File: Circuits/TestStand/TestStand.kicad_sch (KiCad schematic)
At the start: 43 parts, among them J1 Screw_Terminal_01x07, J2 Screw_Terminal_01x07, J3 Screw_Terminal_01x07, J4 Raspberry_Pi_2_3, Q1 MMBT4403-7-F, Q2 MMBT4403-7-F, Q3 MMBT4403-7-F, U1 HX711, U2 HX711, U3 HX711

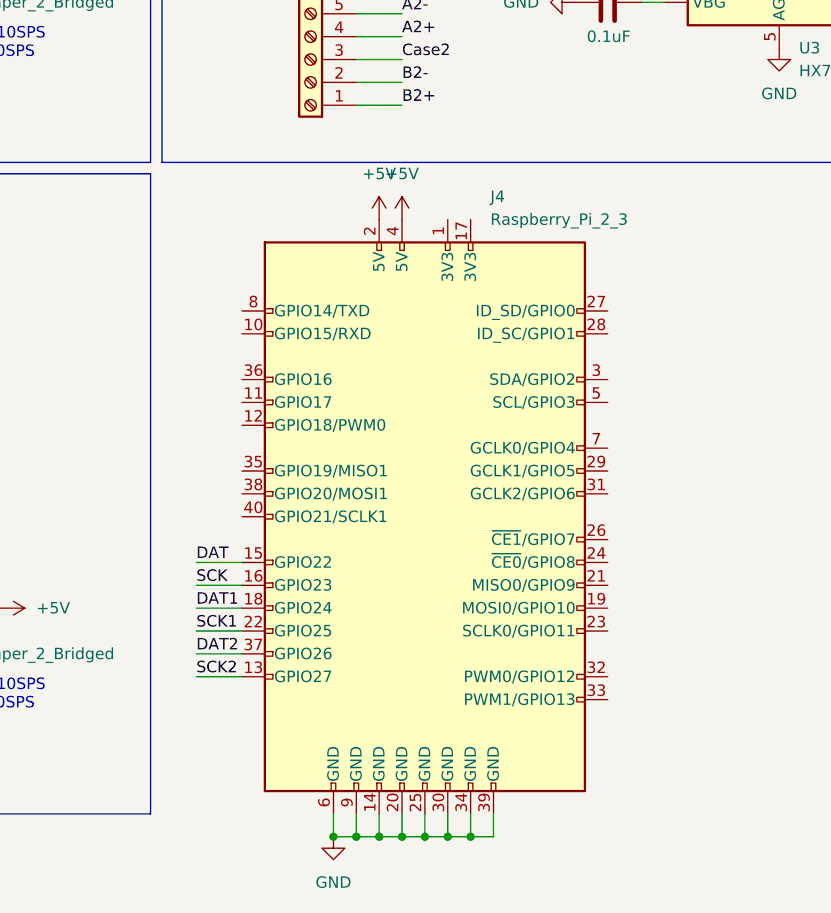
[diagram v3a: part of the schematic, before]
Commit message: Deleted PI, added servos
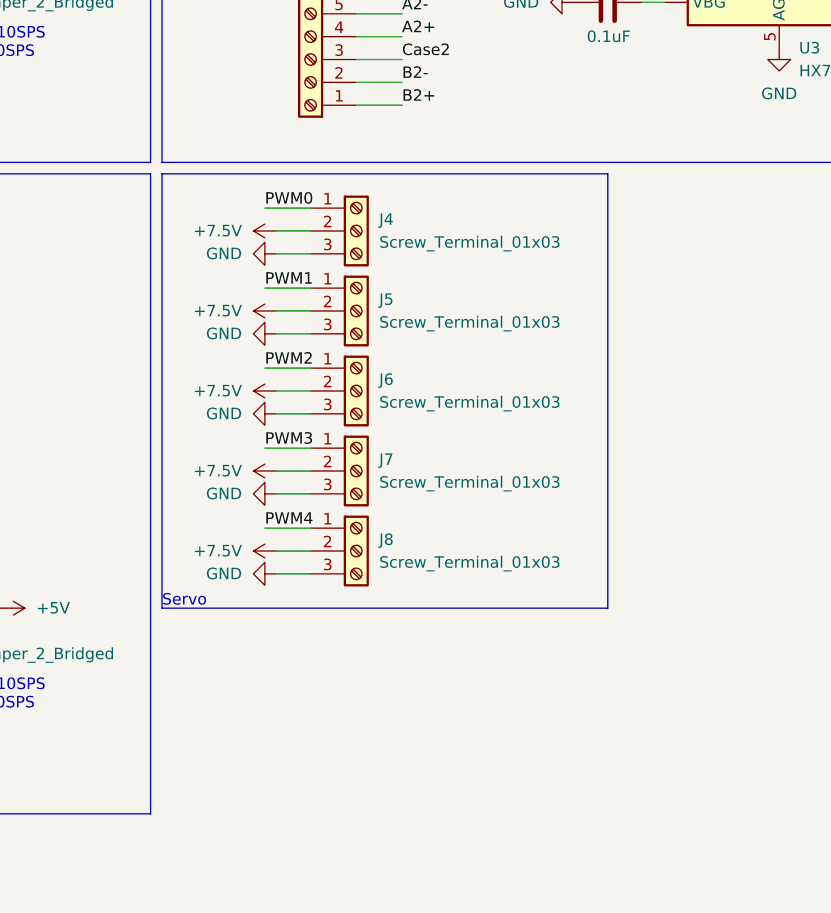
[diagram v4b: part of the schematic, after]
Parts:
- removed J4: Raspberry_Pi_2_3, symbol Connector:Raspberry_Pi_2_3
- added J4, J5, J6, J7, J8: Screw_Terminal_01x03, symbol Connector:Screw_Terminal_01x03
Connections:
- net GND: now also J4.3 (Pin_3), J5.3 (Pin_3), J6.3 (Pin_3), J7.3 (Pin_3), J8.3 (Pin_3)
- new net +7.5V: J4.2 (Pin_2), J5.2 (Pin_2), J6.2 (Pin_2), J7.2 (Pin_2), J8.2 (Pin_2)
- new net PWM0: J4.1 (Pin_1)
- new net PWM1: J5.1 (Pin_1)
- new net PWM2: J6.1 (Pin_1)
- new net PWM3: J7.1 (Pin_1)
- new net PWM4: J8.1 (Pin_1)
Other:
- note added: "Servo"

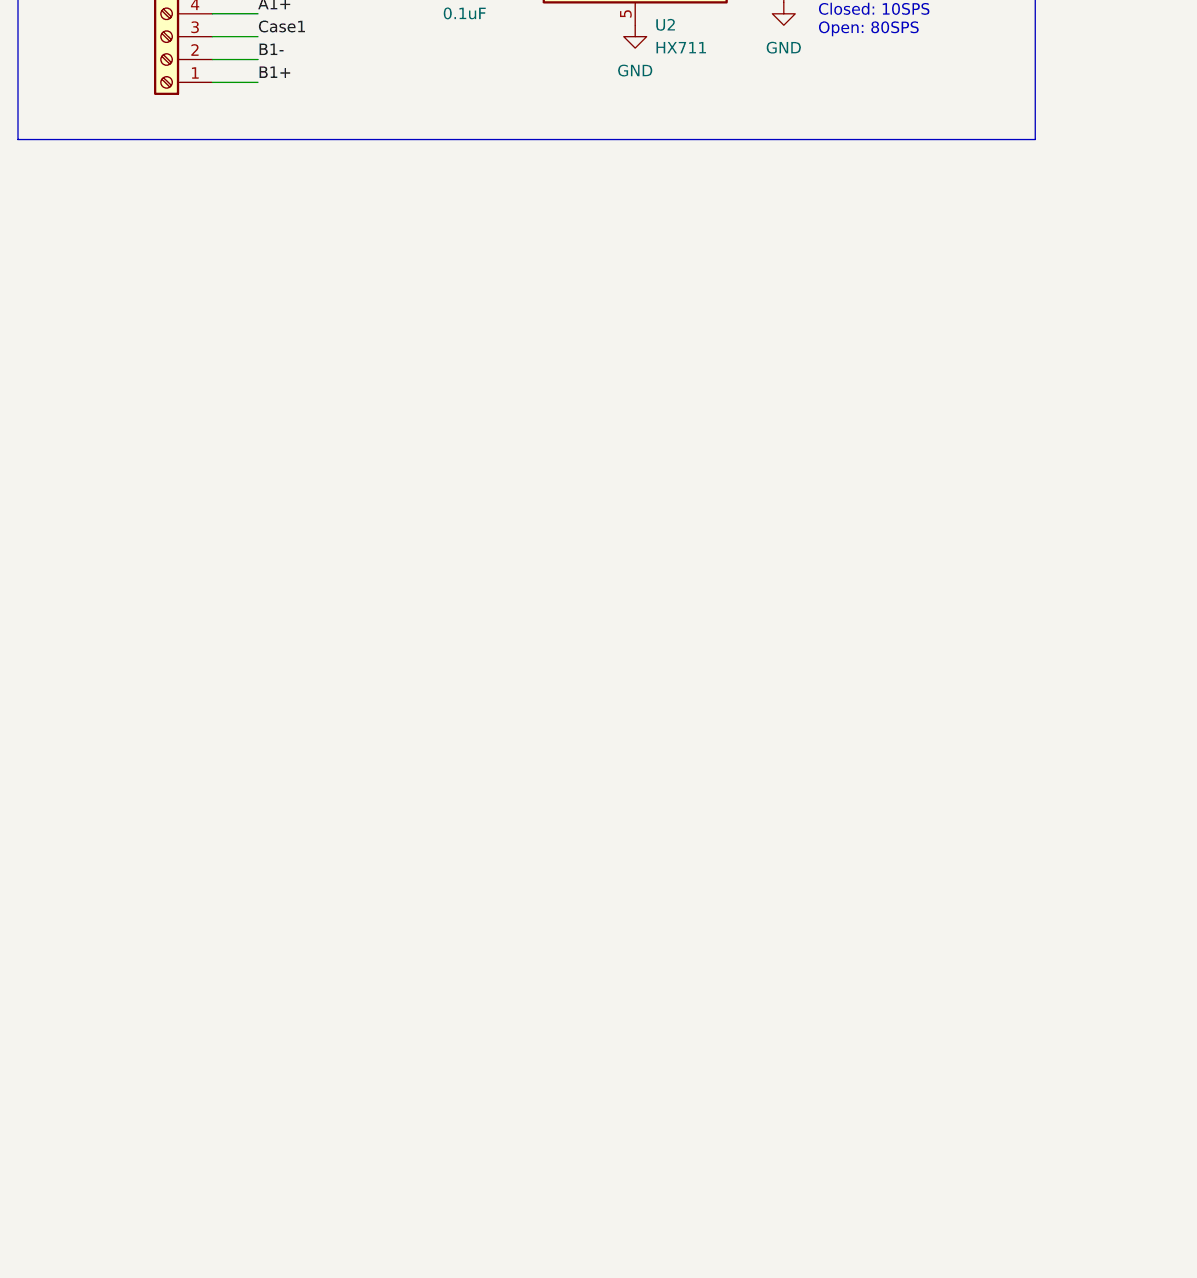
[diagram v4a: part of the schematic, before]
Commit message: Added TEENSY libraries and teensy to schematic
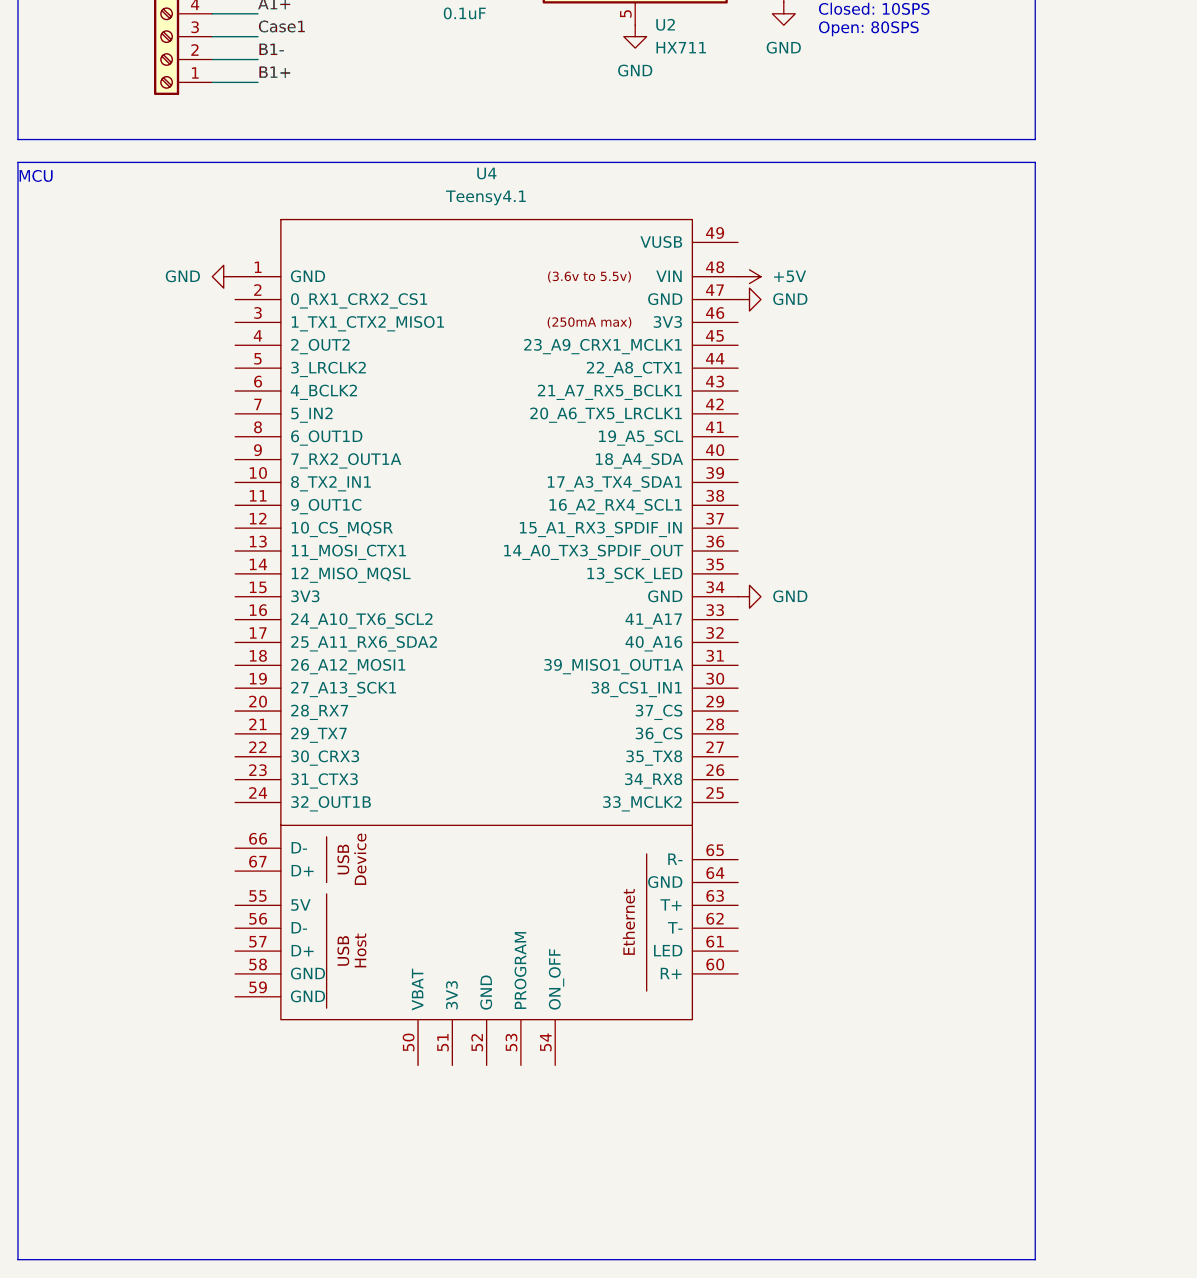
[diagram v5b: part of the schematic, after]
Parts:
- added U4: Teensy4.1, symbol teensy:Teensy4.1
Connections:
- net +5V: now also U4.48 (VIN)
- net GND: now also U4.1 (GND), U4.34 (GND), U4.47 (GND)
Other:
- note added: "MCU"
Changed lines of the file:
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@@
 (kicad_sch (version 20230121) (generator eeschema)
-  (paper "A4")
+  (paper "E")
   (junction (at 101.6 138.43) (diameter 0) (color 0 0 0 0)
   )
@@
     (stroke (width 0) (type default))
   )
+  (rectangle (start 16.51 163.83) (end 129.54 285.75)
+    (stroke (width 0) (type default))
+    (fill (type none))
+  )
   (rectangle (start 130.81 17.78) (end 243.84 88.9)
     (stroke (width 0) (type default))
@@
   )
   (text "Closed: 10SPS\nOpen: 80SPS" (at 105.41 77.47 0)
+    (effects (font (size 1.27 1.27)) (justify left bottom))
+  )
+  (text "MCU" (at 16.51 166.37 0)
     (effects (font (size 1.27 1.27)) (justify left bottom))
   )
@@
         (path "/685411e9-e044-4af3-ae59-8bb36f8f4098"
           (reference "J2") (unit 1)
+        )
+      )
+    )
+  )
+  (symbol (lib_id "power:+5V") (at 96.52 176.53 270) (unit 1)
+    (in_bom yes) (on_board yes) (dnp no) (fields_autoplaced)
+    (property "Reference" "#PWR047" (at 92.71 176.53 0)
+      (effects (font (size 1.27 1.27)) hide)
+    )
+    (property "Value" "+5V" (at 100.33 176.53 90)
+      (effects (font (size 1.27 1.27)) (justify left))
+    )
+    (property "Footprint" "" (at 96.52 176.53 0)
+      (effects (font (size 1.27 1.27)) hide)
+    )
+    (property "Datasheet" "" (at 96.52 176.53 0)
+      (effects (font (size 1.27 1.27)) hide)
+    )
+    (pin "1")
+    (instances
+      (project "TestStand"
+        (path "/685411e9-e044-4af3-ae59-8bb36f8f4098"
+          (reference "#PWR047") (unit 1)
         )
       )
@@
     )
   )
+  (symbol (lib_id "power:GND") (at 40.64 176.53 270) (unit 1)
+    (in_bom yes) (on_board yes) (dnp no) (fields_autoplaced)
+    (property "Reference" "#PWR049" (at 34.29 176.53 0)
+      (effects (font (size 1.27 1.27)) hide)
+    )
+    (property "Value" "GND" (at 36.83 176.53 90)
+      (effects (font (size 1.27 1.27)) (justify right))
+    )
+    (property "Footprint" "" (at 40.64 176.53 0)
+      (effects (font (size 1.27 1.27)) hide)
+    )
+    (property "Datasheet" "" (at 40.64 176.53 0)
+      (effects (font (size 1.27 1.27)) hide)
+    )
+    (pin "1")
+    (instances
+      (project "TestStand"
+        (path "/685411e9-e044-4af3-ae59-8bb36f8f4098"
+          (reference "#PWR049") (unit 1)
+        )
+      )
+    )
+  )
+  (symbol (lib_id "power:GND") (at 96.52 179.07 90) (unit 1)
+    (in_bom yes) (on_board yes) (dnp no) (fields_autoplaced)
+    (property "Reference" "#PWR048" (at 102.87 179.07 0)
+      (effects (font (size 1.27 1.27)) hide)
+    )
+    (property "Value" "GND" (at 100.33 179.07 90)
+      (effects (font (size 1.27 1.27)) (justify right))
+    )
+    (property "Footprint" "" (at 96.52 179.07 0)
+      (effects (font (size 1.27 1.27)) hide)
+    )
+    (property "Datasheet" "" (at 96.52 179.07 0)
+      (effects (font (size 1.27 1.27)) hide)
+    )
+    (pin "1")
+    (instances
+      (project "TestStand"
+        (path "/685411e9-e044-4af3-ae59-8bb36f8f4098"
+          (reference "#PWR048") (unit 1)
+        )
+      )
+    )
+  )
   (symbol (lib_id "Connector:Screw_Terminal_01x03") (at 152.4 132.08 0) (unit 1)
     (in_bom yes) (on_board yes) (dnp no) (fields_autoplaced)
@@
     )
   )
+  (symbol (lib_id "power:GND") (at 96.52 212.09 90) (unit 1)
+    (in_bom yes) (on_board yes) (dnp no) (fields_autoplaced)
+    (property "Reference" "#PWR050" (at 102.87 212.09 0)
+      (effects (font (size 1.27 1.27)) hide)
+    )
+    (property "Value" "GND" (at 100.33 212.09 90)
+      (effects (font (size 1.27 1.27)) (justify right))
+    )
+    (property "Footprint" "" (at 96.52 212.09 0)
+      (effects (font (size 1.27 1.27)) hide)
+    )
+    (property "Datasheet" "" (at 96.52 212.09 0)
+      (effects (font (size 1.27 1.27)) hide)
+    )
+    (pin "1")
+    (instances
+      (project "TestStand"
+        (path "/685411e9-e044-4af3-ae59-8bb36f8f4098"
+          (reference "#PWR050") (unit 1)
+        )
+      )
+    )
+  )
   (symbol (lib_id "Device:R_US") (at 109.22 66.04 90) (unit 1)
     (in_bom yes) (on_board yes) (dnp no) (fields_autoplaced)
@@
         )
       )
+    )
+  )
+  (symbol (lib_id "teensy:Teensy4.1") (at 68.58 231.14 0) (unit 1)
+    (in_bom yes) (on_board yes) (dnp no) (fields_autoplaced)
+    (property "Reference" "U4" (at 68.58 165.1 0)
+      (effects (font (size 1.27 1.27)))
+    )
+    (property "Value" "Teensy4.1" (at 68.58 167.64 0)
+      (effects (font (size 1.27 1.27)))
+    )
+    (property "Footprint" "" (at 58.42 220.98 0)
+      (effects (font (size 1.27 1.27)) hide)
+    )
+    (property "Datasheet" "" (at 58.42 220.98 0)
+      (effects (font (size 1.27 1.27)) hide)
+    )
+    (pin "1")
+    (pin "2")
+    (pin "9")
+    (pin "53")
+    (pin "39")
+    (pin "22")
+    (pin "28")
+    (pin "33")
+    (pin "40")
+    (pin "37")
+    (pin "45")
+    (pin "16")
+    (pin "14")
+    (pin "20")
+    (pin "21")
+    (pin "25")
+    (pin "32")
+    (pin "11")
+    (pin "29")
+    (pin "41")
+    (pin "49")
+    (pin "5")
+    (pin "31")
+    (pin "35")
+    (pin "51")
+    (pin "24")
+    (pin "47")
+    (pin "52")
+    (pin "55")
+    (pin "56")
+    (pin "57")
+    (pin "59")
+    (pin "6")
+    (pin "62")
+    (pin "64")
+    (pin "50")
+    (pin "65")
+    (pin "38")
+    (pin "43")
+    (pin "66")
+    (pin "67")
+    (pin "18")
+    (pin "19")
+    (pin "23")
+    (pin "13")
+    (pin "54")
+    (pin "12")
+    (pin "63")
+    (pin "26")
+    (pin "44")
+    (pin "7")
+    (pin "15")
+    (pin "46")
+    (pin "10")
+    (pin "27")
+    (pin "30")
+    (pin "36")
+    (pin "42")
+    (pin "48")
+    (pin "58")
+    (pin "61")
+    (pin "8")
+    (pin "17")
+    (pin "60")
+    (pin "3")
+    (pin "4")
+    (pin "34")
+    (instances
+      (project "TestStand"
+        (path "/685411e9-e044-4af3-ae59-8bb36f8f4098"
+          (reference "U4") (unit 1)
+        )
+      )
